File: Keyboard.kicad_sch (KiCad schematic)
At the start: 12 parts, among them SW1 SW_SPDT, U1 MCP23017_SO, U2 MCP23017_SO, U3 Seeeduino Xiao nRF52840

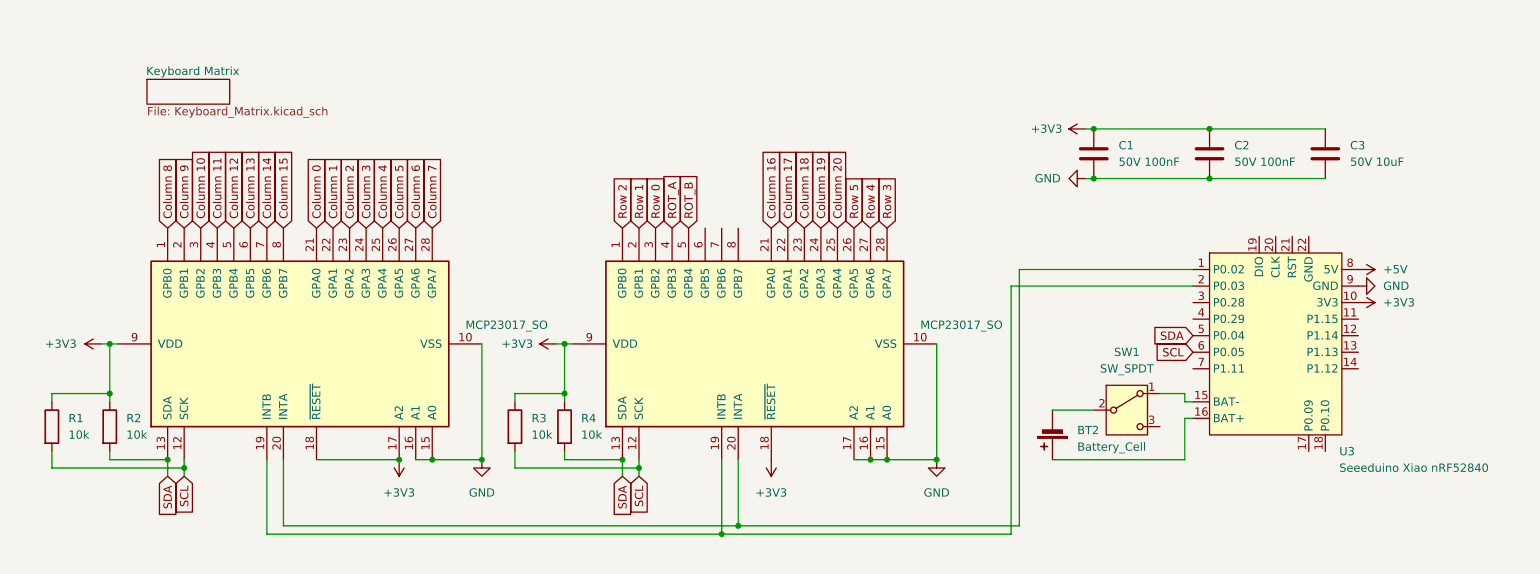
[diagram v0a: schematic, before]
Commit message: Added the OLED SPI Display and remade the entire PCB
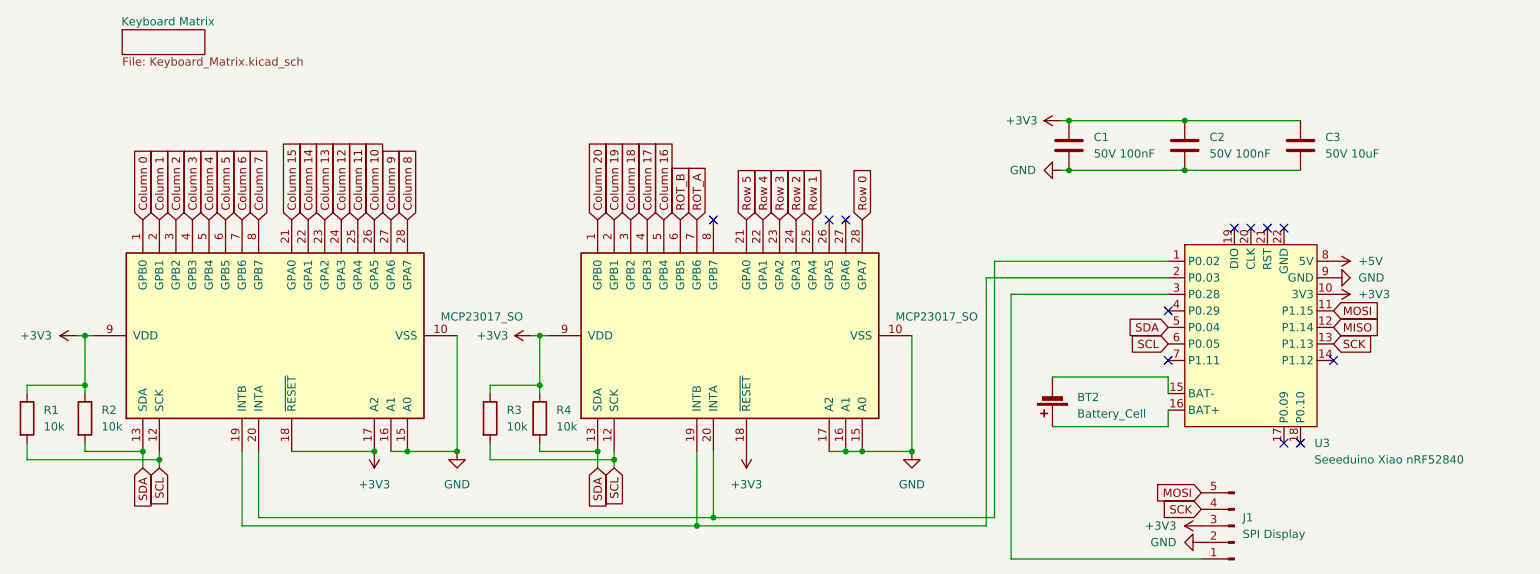
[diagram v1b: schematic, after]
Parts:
- removed SW1: SW_SPDT, Button_Switch_SMD:SW_SPDT_PCM12, symbol Switch:SW_SPDT
- added J1: SPI Display, symbol Connector:Conn_01x05_Pin
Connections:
- net +3V3: now also J1.3 (Pin_3)
- net Column 0: now also U1.1 (GPB0); no longer U1.21 (GPA0)
- net Column 1: now also U1.2 (GPB1); no longer U1.22 (GPA1)
- net Column 10: now also U1.26 (GPA5); no longer U1.3 (GPB2)
- net Column 11: now also U1.25 (GPA4); no longer U1.4 (GPB3)
- net Column 12: now also U1.24 (GPA3); no longer U1.5 (GPB4)
- net Column 13: now also U1.23 (GPA2); no longer U1.6 (GPB5)
- net Column 14: now also U1.22 (GPA1); no longer U1.7 (GPB6)
- net Column 15: now also U1.21 (GPA0); no longer U1.8 (GPB7)
- net Column 16: now also U2.5 (GPB4); no longer U2.21 (GPA0)
- net Column 17: now also U2.4 (GPB3); no longer U2.22 (GPA1)
- net Column 18: now also U2.3 (GPB2); no longer U2.23 (GPA2)
- net Column 19: now also U2.2 (GPB1); no longer U2.24 (GPA3)
- net Column 2: now also U1.3 (GPB2); no longer U1.23 (GPA2)
- net Column 20: now also U2.1 (GPB0); no longer U2.25 (GPA4)
- net Column 3: now also U1.4 (GPB3); no longer U1.24 (GPA3)
- net Column 4: now also U1.5 (GPB4); no longer U1.25 (GPA4)
- net Column 5: now also U1.6 (GPB5); no longer U1.26 (GPA5)
- net Column 6: now also U1.7 (GPB6); no longer U1.27 (GPA6)
- net Column 7: now also U1.8 (GPB7); no longer U1.28 (GPA7)
- net Column 8: now also U1.28 (GPA7); no longer U1.1 (GPB0)
- net Column 9: now also U1.27 (GPA6); no longer U1.2 (GPB1)
- net GND: now also J1.2 (Pin_2)
- net ROT_A: now also U2.7 (GPB6); no longer U2.4 (GPB3)
- net ROT_B: now also U2.6 (GPB5); no longer U2.5 (GPB4)
- net Row 0: now also U2.28 (GPA7); no longer U2.3 (GPB2)
- net Row 1: now also U2.25 (GPA4); no longer U2.2 (GPB1)
- net Row 2: now also U2.24 (GPA3); no longer U2.1 (GPB0)
- net Row 3: now also U2.23 (GPA2); no longer U2.28 (GPA7)
- net Row 4: now also U2.22 (GPA1); no longer U2.27 (GPA6)
- net Row 5: now also U2.21 (GPA0); no longer U2.26 (GPA5)
- net at U3.15 (BAT-): now also BT2.2 (-)
- net MOSI: now reaches U3.11 (P1.15)
- net MOSI: now also J1.5 (Pin_5)
- net MISO: now reaches U3.12 (P1.14)
- net SCK: now reaches U3.13 (P1.13)
- net SCK: now also J1.4 (Pin_4)
- net at U3.3 (P0.28): now also J1.1 (Pin_1)
- no-connect marks 0 -> 12
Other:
- moved on the sheet: BT2, C1, C2, C3, R1, R2, R3, R4, U3

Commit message: Fixed battery symbol errors.
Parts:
- renumbered BT2 to BT1
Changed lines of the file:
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@@
 		(exclude_from_sim no)
 		(in_bom yes)
-		(on_board yes)
+		(on_board no)
 		(dnp no)
-		(property "Reference" "BT2"
+		(property "Reference" "BT1"
 			(at 200.66 98.3614 0)
 			(effects
@@
 			(project ""
 				(path "/196ff9a7-f83d-4312-a11a-1b8b06a0fc5c"
-					(reference "BT2")
+					(reference "BT1")
 					(unit 1)
 				)
